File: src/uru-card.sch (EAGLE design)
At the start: 40 parts, among them U1 ESP32-PICO-D4, U2 MPR121QR2, U3 AP2112K-3.3TRG1, U6 ATECC508A-UDFN

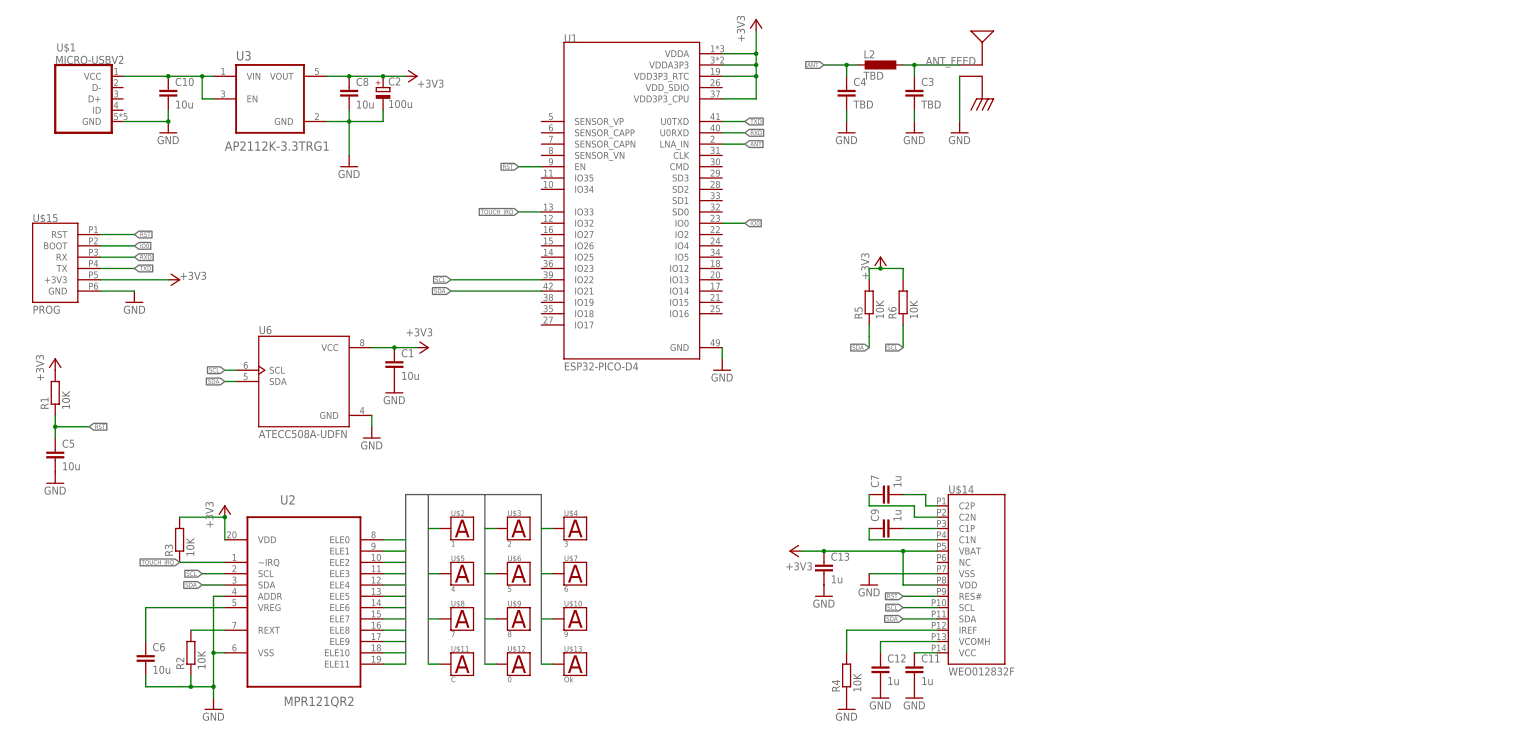
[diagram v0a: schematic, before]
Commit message: Added FT260Q USB I2C
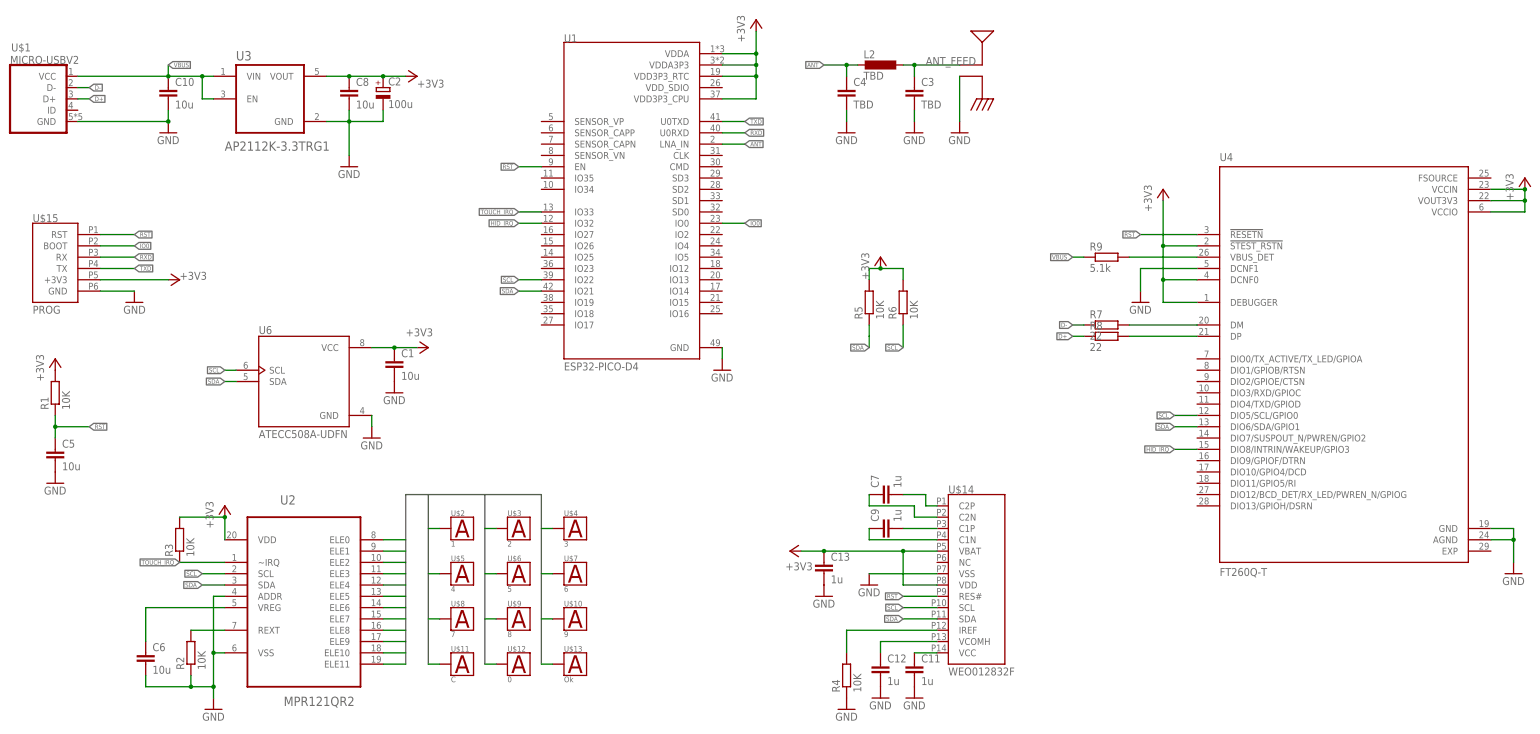
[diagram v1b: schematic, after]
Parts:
- added R7, R8: 22, rcl:R-EU_R0603
- added R9: 5.1k, rcl:R-EU_R0603
- added U4: FT260Q-T, FT260Q-T:FT260Q-T
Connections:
- removed net VCC: C10.1, U$1.VCC, U3.EN, U3.VIN
- new net D+: R8.1, U$1.D+
- new net D-: R7.1, U$1.D-
- new net HID_IRQ: U1.IO32, U4.DIO8/INTRIN/WAKEUP/GPIO3
- new net N$17: R9.2, U4.VBUS_DET
- new net N$5: R7.2, U4.DM
- new net N$9: R8.2, U4.DP
- new net VBUS: C10.1, R9.1, U$1.VCC, U3.EN, U3.VIN
- net +3V3: now also U4.!STEST_RSTN, U4.DCNF0, U4.DEBUGGER, U4.VCCIN, U4.VCCIO, U4.VOUT3V3
- net GND: now also U4.AGND, U4.DCNF1, U4.GND
- net RST: now also U4.!RESETN
- net SCL: now also U4.DIO5/SCL/GPIO0
- net SDA: now also U4.DIO6/SDA/GPIO1
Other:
- moved on the sheet: U$1

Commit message: Changed routing for the display component
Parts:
- U$14: value WEO012832F -> WEO012832FREVERSED; device OLED:WEO012832F -> OLED:WEO012832FREVERSED
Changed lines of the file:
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@@
 <grid distance="0.1" unitdist="inch" unit="inch" style="lines" multiple="1" display="no" altdistance="0.01" altunitdist="inch" altunit="inch"/>
 <layers>
-<layer number="1" name="Top" color="4" fill="1" visible="no" active="no"/>
-<layer number="16" name="Bottom" color="1" fill="1" visible="no" active="no"/>
-<layer number="17" name="Pads" color="2" fill="1" visible="no" active="no"/>
-<layer number="18" name="Vias" color="2" fill="1" visible="no" active="no"/>
-<layer number="19" name="Unrouted" color="6" fill="1" visible="no" active="no"/>
-<layer number="20" name="Dimension" color="24" fill="1" visible="no" active="no"/>
-<layer number="21" name="tPlace" color="7" fill="1" visible="no" active="no"/>
-<layer number="22" name="bPlace" color="7" fill="1" visible="no" active="no"/>
-<layer number="23" name="tOrigins" color="15" fill="1" visible="no" active="no"/>
-<layer number="24" name="bOrigins" color="15" fill="1" visible="no" active="no"/>
-<layer number="25" name="tNames" color="7" fill="1" visible="no" active="no"/>
-<layer number="26" name="bNames" color="7" fill="1" visible="no" active="no"/>
-<layer number="27" name="tValues" color="7" fill="1" visible="no" active="no"/>
-<layer number="28" name="bValues" color="7" fill="1" visible="no" active="no"/>
+<layer number="1" name="Top" color="4" fill="1" visible="yes" active="no"/>
+<layer number="16" name="Bottom" color="1" fill="1" visible="yes" active="no"/>
+<layer number="17" name="Pads" color="2" fill="1" visible="yes" active="no"/>
+<layer number="18" name="Vias" color="2" fill="1" visible="yes" active="no"/>
+<layer number="19" name="Unrouted" color="6" fill="1" visible="yes" active="no"/>
+<layer number="20" name="Dimension" color="24" fill="1" visible="yes" active="no"/>
+<layer number="21" name="tPlace" color="7" fill="1" visible="yes" active="no"/>
+<layer number="22" name="bPlace" color="7" fill="1" visible="yes" active="no"/>
+<layer number="23" name="tOrigins" color="15" fill="1" visible="yes" active="no"/>
+<layer number="24" name="bOrigins" color="15" fill="1" visible="yes" active="no"/>
+<layer number="25" name="tNames" color="7" fill="1" visible="yes" active="no"/>
+<layer number="26" name="bNames" color="7" fill="1" visible="yes" active="no"/>
+<layer number="27" name="tValues" color="7" fill="1" visible="yes" active="no"/>
+<layer number="28" name="bValues" color="7" fill="1" visible="yes" active="no"/>
 <layer number="29" name="tStop" color="7" fill="3" visible="no" active="no"/>
 <layer number="30" name="bStop" color="7" fill="6" visible="no" active="no"/>
@@
 <layer number="35" name="tGlue" color="7" fill="4" visible="no" active="no"/>
 <layer number="36" name="bGlue" color="7" fill="5" visible="no" active="no"/>
-<layer number="37" name="tTest" color="7" fill="1" visible="no" active="no"/>
-<layer number="38" name="bTest" color="7" fill="1" visible="no" active="no"/>
+<layer number="37" name="tTest" color="7" fill="1" visible="yes" active="no"/>
+<layer number="38" name="bTest" color="7" fill="1" visible="yes" active="no"/>
 <layer number="39" name="tKeepout" color="4" fill="11" visible="no" active="no"/>
 <layer number="40" name="bKeepout" color="1" fill="11" visible="no" active="no"/>
@@
 <layer number="44" name="Drills" color="7" fill="1" visible="no" active="no"/>
 <layer number="45" name="Holes" color="7" fill="1" visible="no" active="no"/>
-<layer number="46" name="Milling" color="3" fill="1" visible="no" active="no"/>
-<layer number="47" name="Measures" color="7" fill="1" visible="no" active="no"/>
-<layer number="48" name="Document" color="7" fill="1" visible="no" active="no"/>
-<layer number="49" name="Reference" color="7" fill="1" visible="no" active="no"/>
-<layer number="50" name="dxf" color="7" fill="1" visible="no" active="no"/>
-<layer number="51" name="tDocu" color="7" fill="1" visible="no" active="no"/>
-<layer number="52" name="bDocu" color="7" fill="1" visible="no" active="no"/>
-<layer number="53" name="tGND_GNDA" color="7" fill="9" visible="no" active="no"/>
-<layer number="54" name="bGND_GNDA" color="1" fill="9" visible="no" active="no"/>
-<layer number="56" name="wert" color="7" fill="1" visible="no" active="no"/>
+<layer number="46" name="Milling" color="3" fill="1" visible="yes" active="no"/>
+<layer number="47" name="Measures" color="7" fill="1" visible="yes" active="no"/>
+<layer number="48" name="Document" color="7" fill="1" visible="yes" active="no"/>
+<layer number="49" name="Reference" color="7" fill="1" visible="yes" active="no"/>
+<layer number="50" name="dxf" color="7" fill="1" visible="yes" active="no"/>
+<layer number="51" name="tDocu" color="7" fill="1" visible="yes" active="no"/>
+<layer number="52" name="bDocu" color="7" fill="1" visible="yes" active="no"/>
+<layer number="53" name="tGND_GNDA" color="7" fill="9" visible="yes" active="no"/>
+<layer number="54" name="bGND_GNDA" color="1" fill="9" visible="yes" active="no"/>
+<layer number="56" name="wert" color="7" fill="1" visible="yes" active="no"/>
 <layer number="88" name="SimResults" color="9" fill="1" visible="yes" active="yes"/>
 <layer number="89" name="SimProbes" color="9" fill="1" visible="yes" active="yes"/>
@@
 <part name="U$12" library="pads" deviceset="TOUCH" device="" value="0"/>
 <part name="U$13" library="pads" deviceset="TOUCH" device="" value="Ok"/>
-<part name="U$14" library="OLED" deviceset="WEO012832F" device=""/>
+<part name="U$14" library="OLED" deviceset="WEO012832F" device="REVERSED" value="WEO012832FREVERSED"/>
 <part name="U$15" library="pads" deviceset="PROG" device=""/>
 <part name="C7" library="rcl" library_urn="urn:adsk.eagle:library:334" deviceset="C-EU" device="C0603" package3d_urn="urn:adsk.eagle:package:23616/2" value="1u"/>

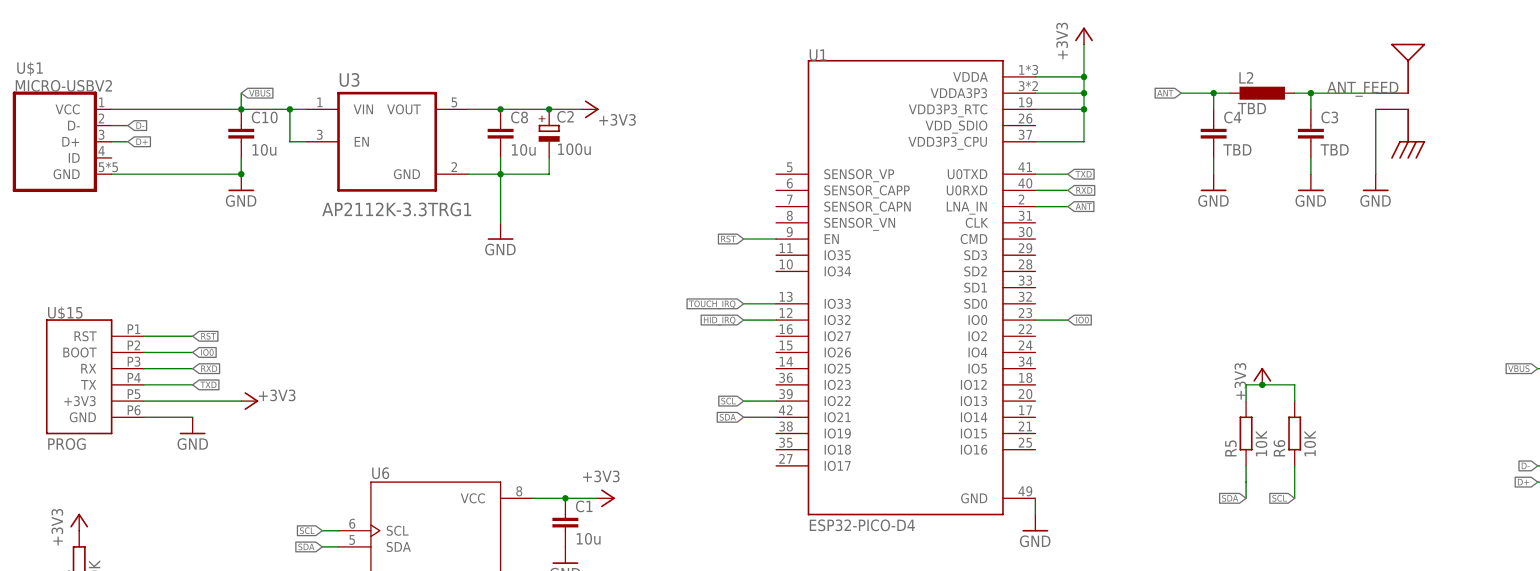
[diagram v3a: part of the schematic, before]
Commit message: Design refactoring
Replaced the antenna with PCB one
Moved connector
Replaced tantalum capacitor with ceramic ones
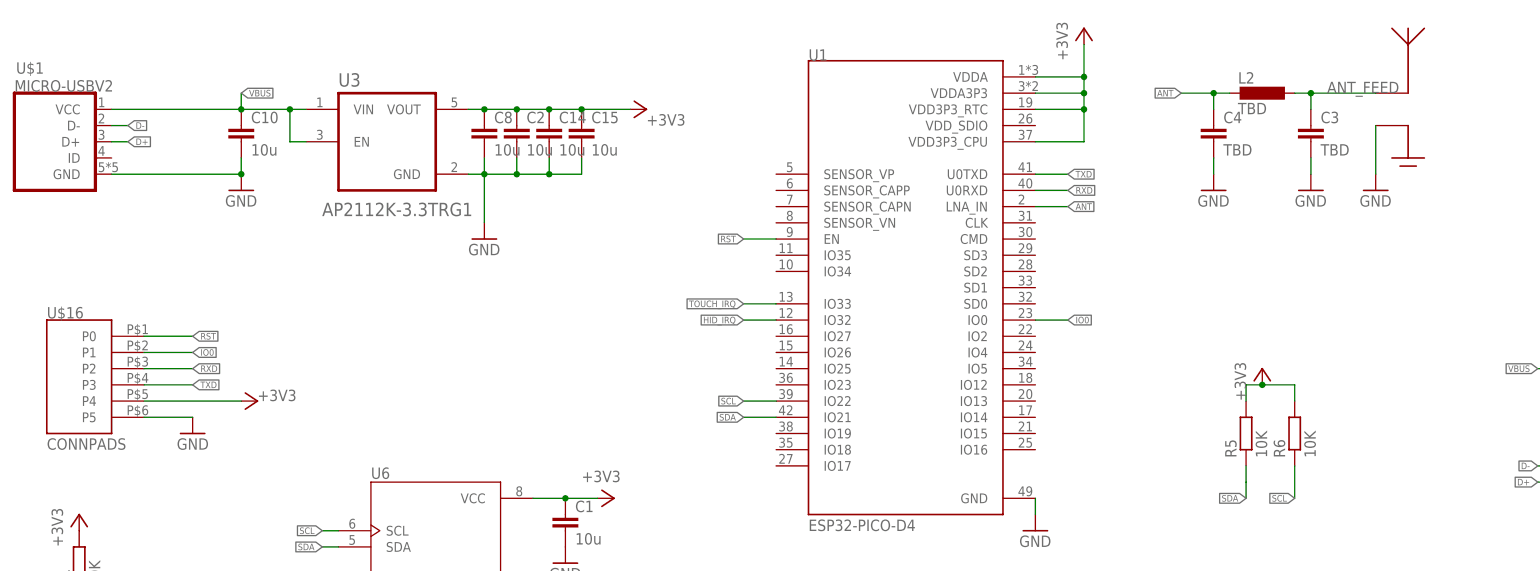
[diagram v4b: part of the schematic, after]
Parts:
- removed ANT1: AN9520, AN9520:AN9520
- added C14, C15: 10u, rcl:C-EUC0603
- added U$16: CONNPADS, CONN:CONNPADS
- C2: value 100u -> 10u; device rcl:CPOL-EUA/3216-18R -> rcl:C-EUC0603
- U$15: value PROG -> ANT-2_4_PCB; device pads:PROG -> ANT:ANT-2_4_PCB
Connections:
- net +3V3: now also C14.1, C15.1, C2.1, U$16.P4; no longer C2.+, U$15.+3V3
- net ANT_FEED: now also U$15.FEED; no longer ANT1.FEED
- net GND: now also C14.2, C15.2, C2.2, U$16.P5; no longer ANT1.GND, C2.-
- net IO0: now also U$16.P1; no longer U$15.BOOT
- net RST: now also U$16.P0; no longer U$15.RST
- net RXD: now also U$16.P2; no longer U$15.RX
- net TXD: now also U$16.P3; no longer U$15.TX
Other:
- moved on the sheet: C8

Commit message: Fixed incorrect connections
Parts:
- R2: value 10K -> 75K
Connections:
- net RXD: now also U1.U0TXD; no longer U1.U0RXD
- net TXD: now also U1.U0RXD; no longer U1.U0TXD
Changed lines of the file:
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@@
 <part name="U2" library="MPR121QR2" deviceset="MPR121QR2" device=""/>
 <part name="C6" library="rcl" library_urn="urn:adsk.eagle:library:334" deviceset="C-EU" device="C0603" package3d_urn="urn:adsk.eagle:package:23616/2" value="10u"/>
-<part name="R2" library="rcl" library_urn="urn:adsk.eagle:library:334" deviceset="R-EU_" device="R0603" package3d_urn="urn:adsk.eagle:package:23555/3" value="10K"/>
+<part name="R2" library="rcl" library_urn="urn:adsk.eagle:library:334" deviceset="R-EU_" device="R0603" package3d_urn="urn:adsk.eagle:package:23555/3" value="75K"/>
 <part name="GND2" library="supply1" library_urn="urn:adsk.eagle:library:371" deviceset="GND" device=""/>
 <part name="R3" library="rcl" library_urn="urn:adsk.eagle:library:334" deviceset="R-EU_" device="R0603" package3d_urn="urn:adsk.eagle:package:23555/3" value="10K"/>
@@
 </segment>
 <segment>
+<pinref part="U1" gate="G$1" pin="U0RXD"/>
+<wire x1="160.02" y1="-38.1" x2="165.1" y2="-38.1" width="0.1524" layer="91"/>
+<label x="165.1" y="-38.1" size="1.016" layer="95" xref="yes"/>
+</segment>
+</net>
+<net name="RXD" class="0">
+<segment>
+<wire x1="20.32" y1="-66.04" x2="27.94" y2="-66.04" width="0.1524" layer="91"/>
+<label x="27.94" y="-66.04" size="1.016" layer="95" xref="yes"/>
+<pinref part="U$16" gate="G$1" pin="P2"/>
+</segment>
+<segment>
 <pinref part="U1" gate="G$1" pin="U0TXD"/>
 <wire x1="160.02" y1="-35.56" x2="165.1" y2="-35.56" width="0.1524" layer="91"/>
@@
 </segment>
 </net>
-<net name="RXD" class="0">
-<segment>
-<wire x1="20.32" y1="-66.04" x2="27.94" y2="-66.04" width="0.1524" layer="91"/>
-<label x="27.94" y="-66.04" size="1.016" layer="95" xref="yes"/>
-<pinref part="U$16" gate="G$1" pin="P2"/>
-</segment>
-<segment>
-<pinref part="U1" gate="G$1" pin="U0RXD"/>
-<wire x1="160.02" y1="-38.1" x2="165.1" y2="-38.1" width="0.1524" layer="91"/>
-<label x="165.1" y="-38.1" size="1.016" layer="95" xref="yes"/>
-</segment>
-</net>

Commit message: Updated CAM job
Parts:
- renumbered U$1 to J1, U$10 to TP9, U$11 to TP10, U$12 to TP11, U$13 to TP12, U$14 to D1, U$16 to J2, U$2 to TP1, U$3 to TP2, U$4 to TP3, U$5 to TP4, U$6 to TP5, U$7 to TP6, U$8 to TP7, U$9 to TP8
